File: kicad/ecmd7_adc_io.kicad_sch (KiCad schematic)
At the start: 84 parts, among them U10 FIN1002M5X, U11 FIN1002M5X, U12 FIN1002M5X, U13 ADM3490ExR, U15 74LVC1G139, U16 MB85RS1MT, U17 TMP122AIDBVR, U2 MCP33151-05T-E/MN, U4 MCP33151-05T-E/MN, U5 MCP33151-05T-E/MN, U7 MCP33151-05T-E/MN

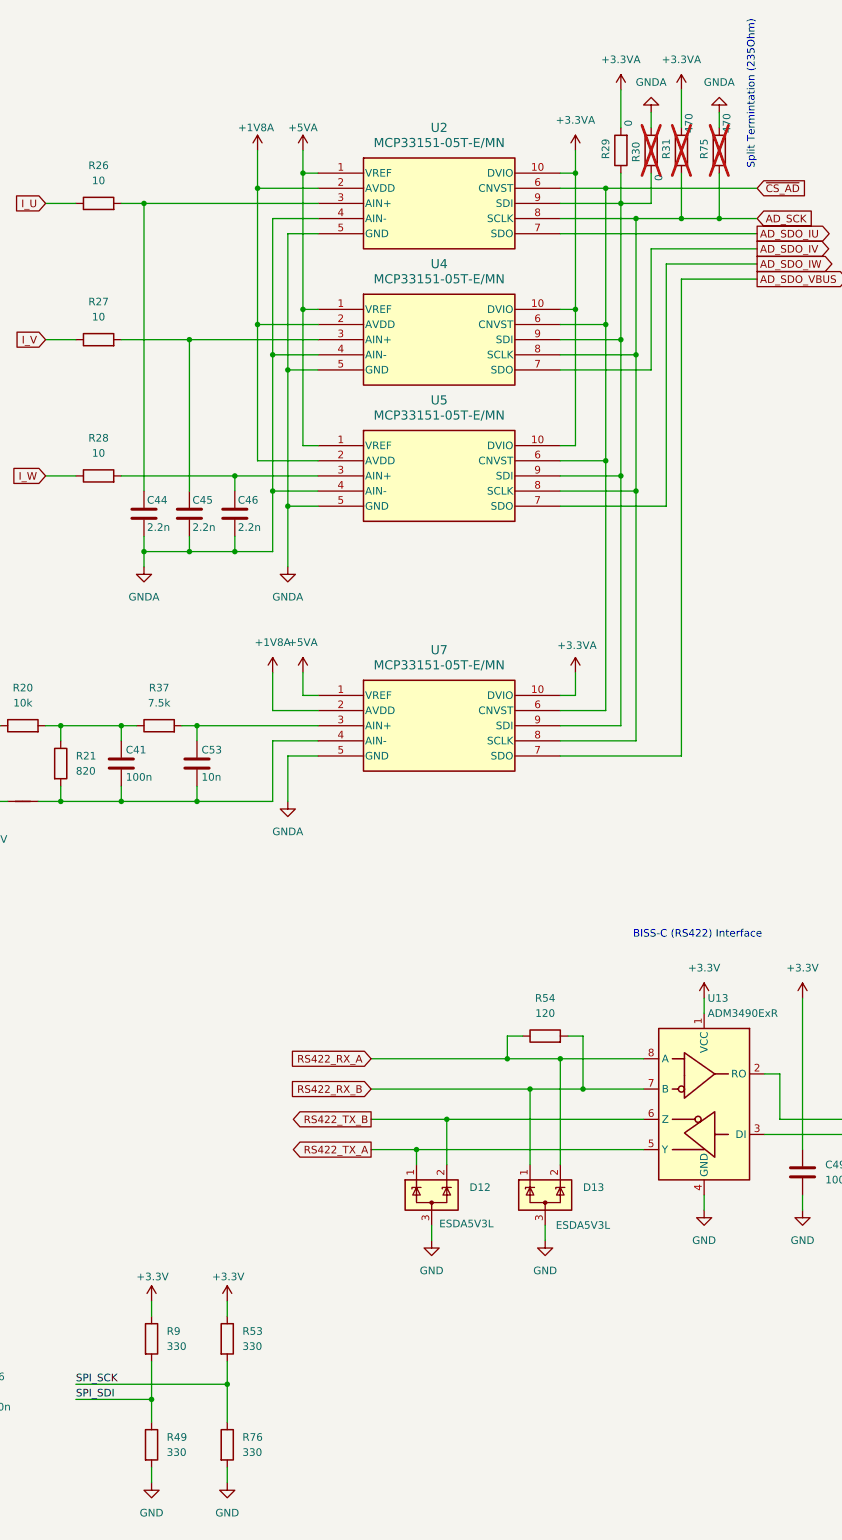
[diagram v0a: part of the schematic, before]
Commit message: Update project structure for enhancment with firmware and software
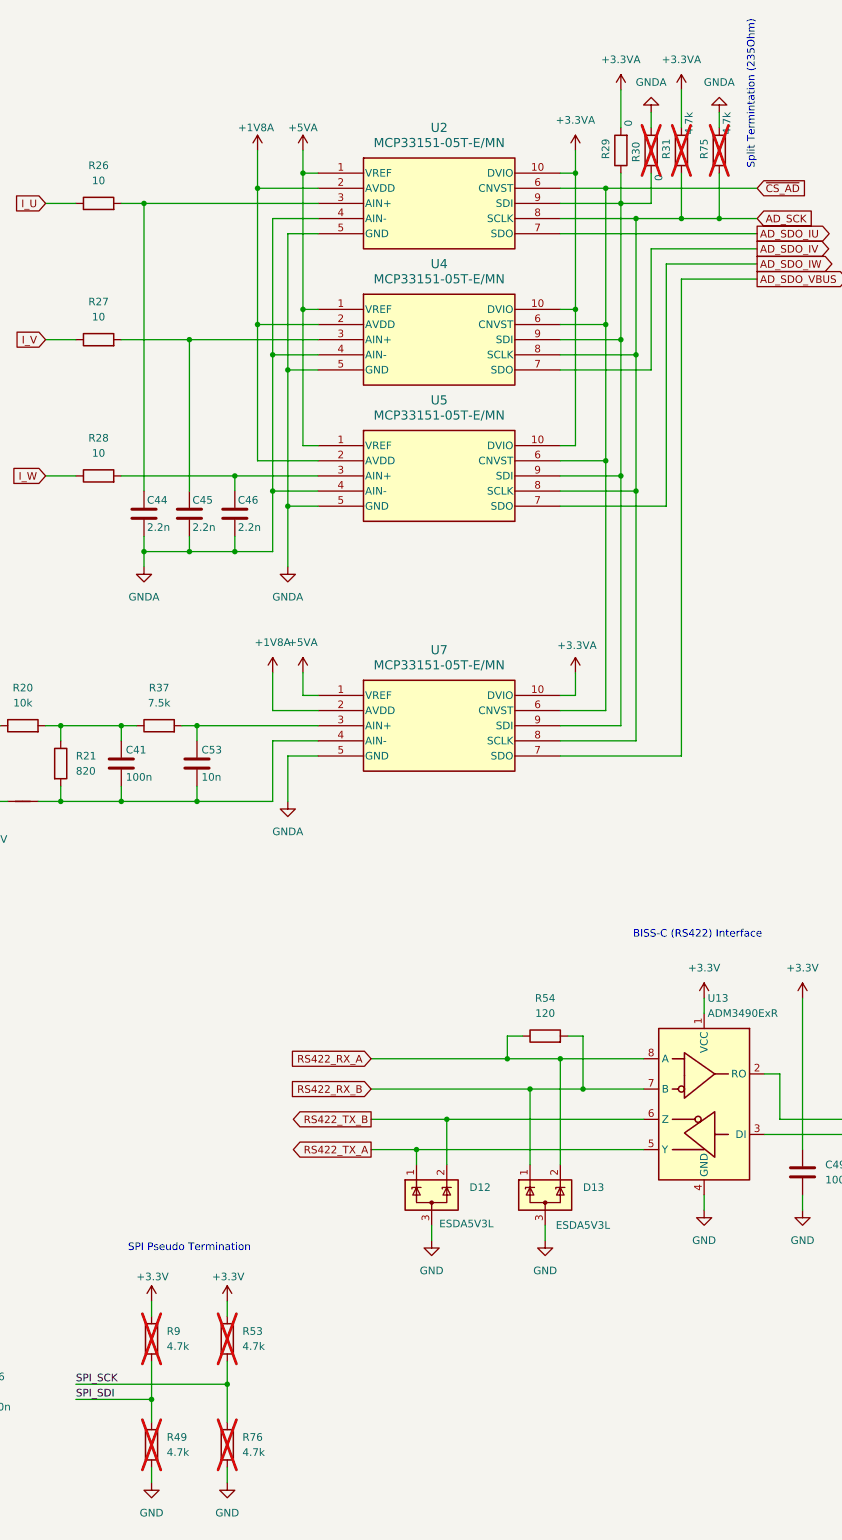
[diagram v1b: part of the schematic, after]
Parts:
- D10, D11, D12, D13, D9: Mouser Part Number (none) -> 511-ESDA5V3L
- R31, R75: value 470 -> 4.7k
- R49, R53, R76, R9: value 330 -> 4.7k; now not fitted
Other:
- note added: "SPI Pseudo Termination"
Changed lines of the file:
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@@
 		(rev "0,0")
 	)
+	(text "SPI Pseudo Termination"
+		(exclude_from_sim no)
+		(at 247.65 222.25 0)
+		(effects
+			(font
+				(size 1.27 1.27)
+			)
+		)
+	)
 	(text "BISS-C (RS422) Interface"
 		(exclude_from_sim no)
@@
 		(in_bom yes)
 		(on_board yes)
-		(dnp no)
+		(dnp yes)
 		(fields_autoplaced yes)
 		(property "Reference" "R53"
@@
 			)
 		)
-		(property "Value" "330"
+		(property "Value" "4.7k"
 			(at 256.54 238.7599 0)
 			(effects
@@
 			)
 		)
+		(property "Mouser Part Number" "511-ESDA5V3L"
+			(at 63.5 181.61 0)
+			(effects
+				(font
+					(size 1.27 1.27)
+				)
+				(hide yes)
+			)
+		)
 		(pin "3"
 		)
@@
 			)
 		)
-		(property "Value" "470"
+		(property "Value" "4.7k"
 			(at 331.47 33.528 90)
 			(effects
@@
 		(in_bom yes)
 		(on_board yes)
-		(dnp no)
+		(dnp yes)
 		(fields_autoplaced yes)
 		(property "Reference" "R9"
@@
 			)
 		)
-		(property "Value" "330"
+		(property "Value" "4.7k"
 			(at 243.84 238.7599 0)
 			(effects
@@
 			)
 		)
+		(property "Mouser Part Number" "511-ESDA5V3L"
+			(at 307.34 213.36 0)
+			(effects
+				(font
+					(size 1.27 1.27)
+				)
+				(hide yes)
+			)
+		)
 		(pin "3"
 		)
@@
 			)
 		)
-		(property "Value" "470"
+		(property "Value" "4.7k"
 			(at 337.82 33.528 90)
 			(effects
@@
 		(in_bom yes)
 		(on_board yes)
-		(dnp no)
+		(dnp yes)
 		(fields_autoplaced yes)
 		(property "Reference" "R76"
@@
 			)
 		)
-		(property "Value" "330"
+		(property "Value" "4.7k"
 			(at 256.54 256.5399 0)
 			(effects
@@
 			)
 		)
+		(property "Mouser Part Number" "511-ESDA5V3L"
+			(at 63.5 68.58 0)
+			(effects
+				(font
+					(size 1.27 1.27)
+				)
+				(hide yes)
+			)
+		)
 		(pin "3"
 		)
@@
 			)
 		)
+		(property "Mouser Part Number" "511-ESDA5V3L"
+			(at 63.5 125.73 0)
+			(effects
+				(font
+					(size 1.27 1.27)
+				)
+				(hide yes)
+			)
+		)
 		(pin "3"
 		)
@@
 			)
 		)
+		(property "Mouser Part Number" "511-ESDA5V3L"
+			(at 288.29 213.36 0)
+			(effects
+				(font
+					(size 1.27 1.27)
+				)
+				(hide yes)
+			)
+		)
 		(pin "3"
 		)
@@
 		(in_bom yes)
 		(on_board yes)
-		(dnp no)
+		(dnp yes)
 		(fields_autoplaced yes)
 		(property "Reference" "R49"
@@
 			)
 		)
-		(property "Value" "330"
+		(property "Value" "4.7k"
 			(at 243.84 256.5399 0)
 			(effects

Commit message: Cleanup schematic
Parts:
- removed C11, C51, C52, C56, C58, C59, C60, C76: 100n, Capacitor_SMD:C_0805_2012Metric, symbol Device:C
- removed C49: 100n, Capacitor_SMD:C_0603_1608Metric, symbol Device:C
- removed D10, D11, D12, D13, D9: ESDA5V3L, Package_TO_SOT_SMD:SOT-23-3, symbol Power_Protection:ESDA5V3L
- removed JP10: ~{WP}=1, Jumper:SolderJumper-2_P1.3mm_Bridged_RoundedPad1.0x1.5mm, symbol Jumper:SolderJumper_2_Bridged
- removed JP12: ~{WP}=0, Jumper:SolderJumper-2_P1.3mm_Open_RoundedPad1.0x1.5mm, symbol Jumper:SolderJumper_2_Open
- removed R22, R23, R24, R25, R39, R40: 3.9k, Resistor_SMD:R_0805_2012Metric, symbol Device:R
- removed R32, R38, R43, R55, R58, R60: 820, Resistor_SMD:R_0805_2012Metric, symbol Device:R
- removed R33, R36, R42: 330, Resistor_SMD:R_0805_2012Metric, symbol Device:R
- removed R34, R35, R41, R56, R57, R59: 1.8k, Resistor_SMD:R_0805_2012Metric, symbol Device:R
- removed R49, R53, R76, R9: 4.7k, Resistor_SMD:R_0805_2012Metric, symbol Device:R
- removed R54: 120, Resistor_SMD:R_0805_2012Metric, symbol Device:R
- removed R61, R62, R63: 100k, Resistor_SMD:R_0805_2012Metric, symbol Device:R
- removed U10, U11, U12: FIN1002M5X, Package_TO_SOT_SMD:SOT-23-5, symbol SSTA:FIN1002M5X
- removed U13: ADM3490ExR, Package_SO:SOIC-8_3.9x4.9mm_P1.27mm, symbol Interface_UART:ADM3490ExR
- removed U15: 74LVC1G139, Package_SO:SSOP-8_2.95x2.8mm_P0.65mm, symbol 74xGxx:74LVC1G139
- removed U16: MB85RS1MT, Package_SO:SOP-8_3.76x4.96mm_P1.27mm, symbol Memory_NVRAM:MB85RS1MT
- removed U17: TMP122AIDBVR, SSTA:DBV6, symbol SSTA:TMP122AIDBVR
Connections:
- no-connect marks 2 -> 0
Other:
- note removed: "BISS-C (RS422) Interface"
- note removed: "Inputs can be configured for differential quadrature encoder signals or hall switches. Default configuration is for differential 5V TTL quadrature encoder inputs"
- note removed: "SPI Pseudo Termination"
- moved on the sheet: C1, C10, C2, C3, C4, C41, C44, C45, C46, C47, C5, C50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

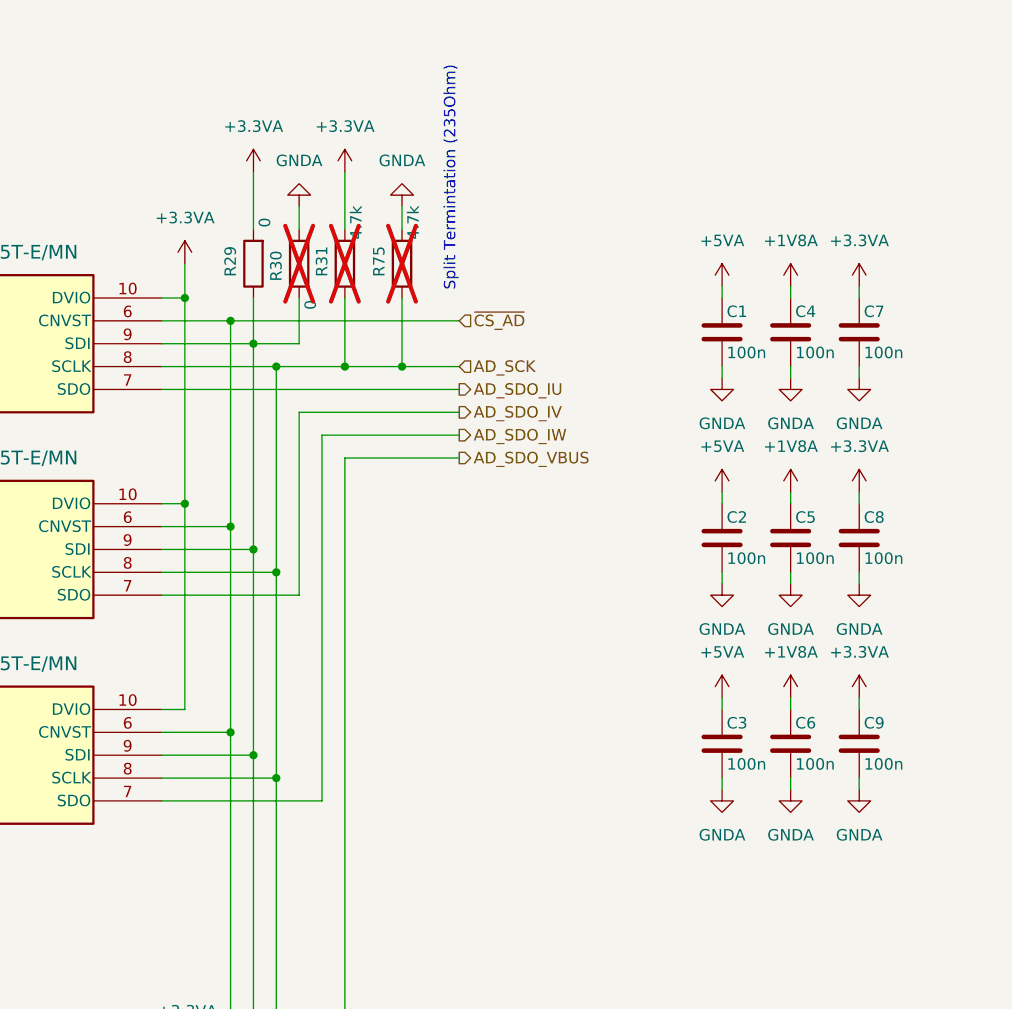
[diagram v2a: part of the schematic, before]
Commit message: Cleanup schematic, add busses
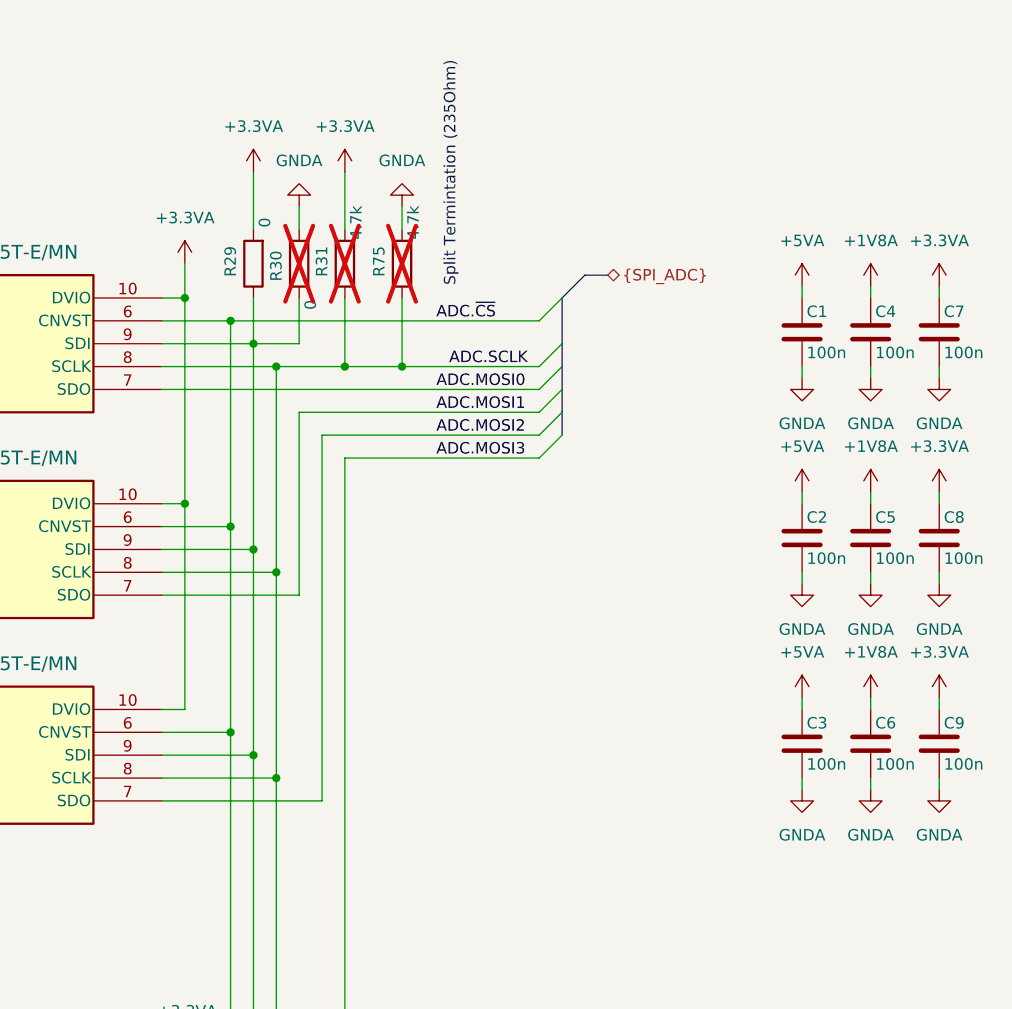
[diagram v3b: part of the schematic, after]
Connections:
- net AD_SCK renamed ADC.SCLK
- net AD_SDO_IU renamed ADC.MOSI0
- net AD_SDO_IV renamed ADC.MOSI1
- net AD_SDO_IW renamed ADC.MOSI2
- net AD_SDO_VBUS renamed ADC.MOSI3
- net ~{CS_AD} renamed ADC.~{CS}
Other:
- title: ECMD7 Feedback -> ECMD7 Current + Voltage Feedback ADC
- moved on the sheet: C1, C2, C3, C4, C5, C6, C7, C8, C9

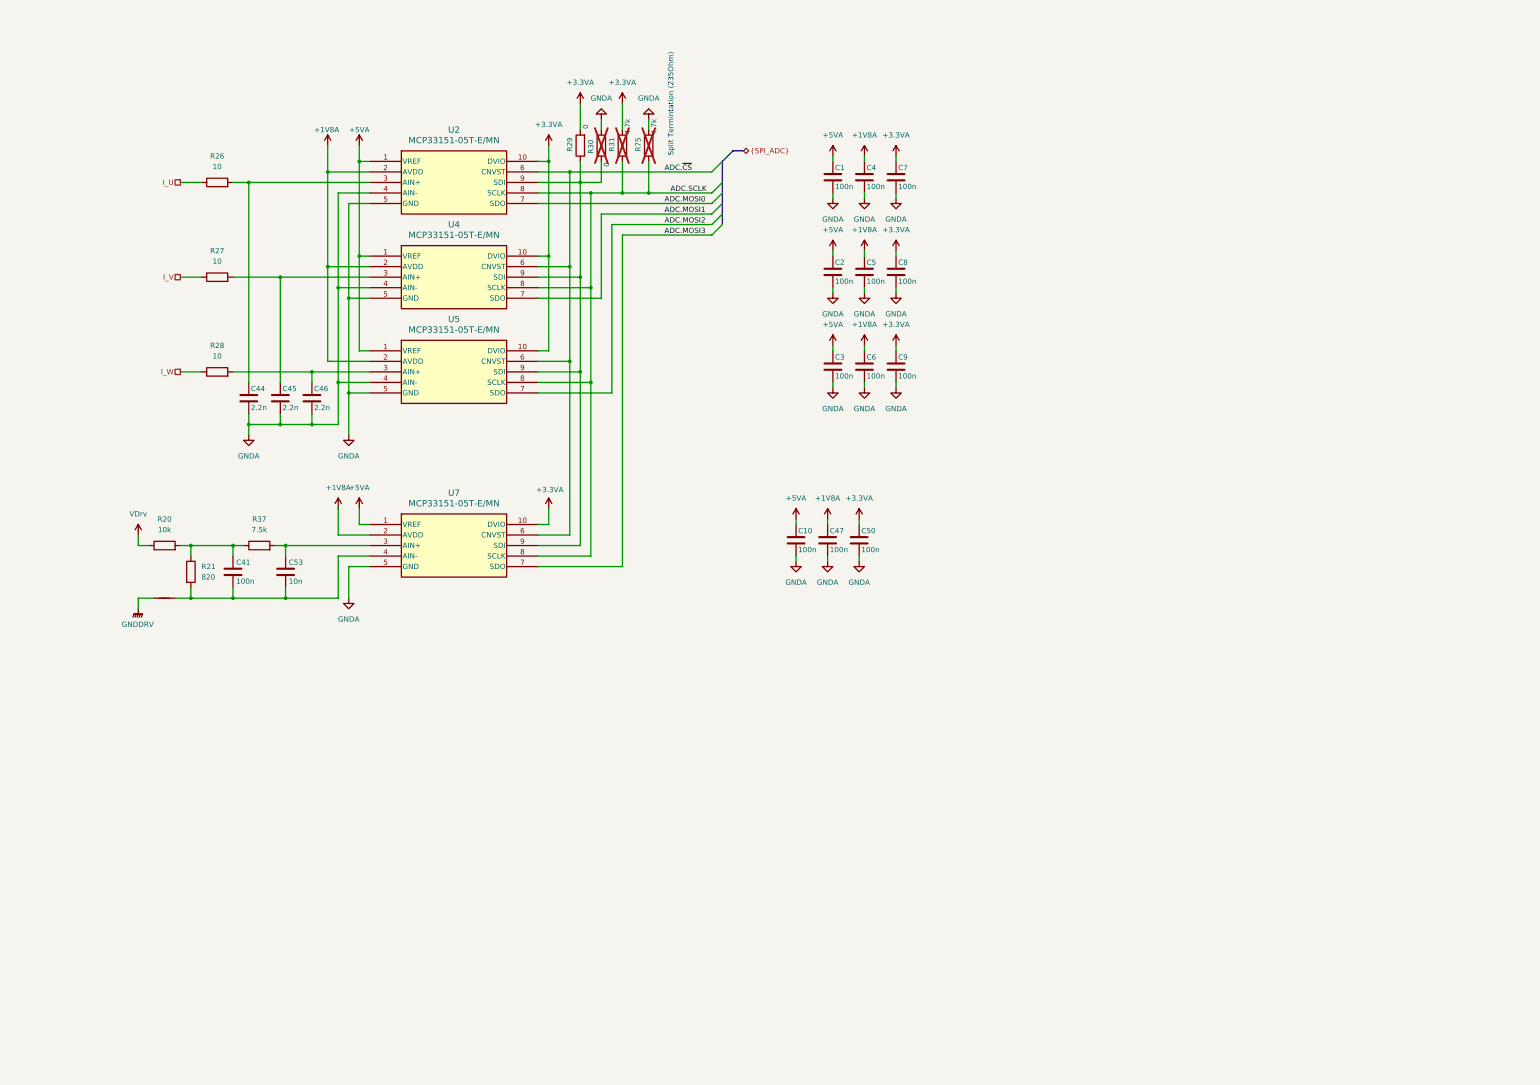
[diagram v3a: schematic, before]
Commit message: General schematic cleanup
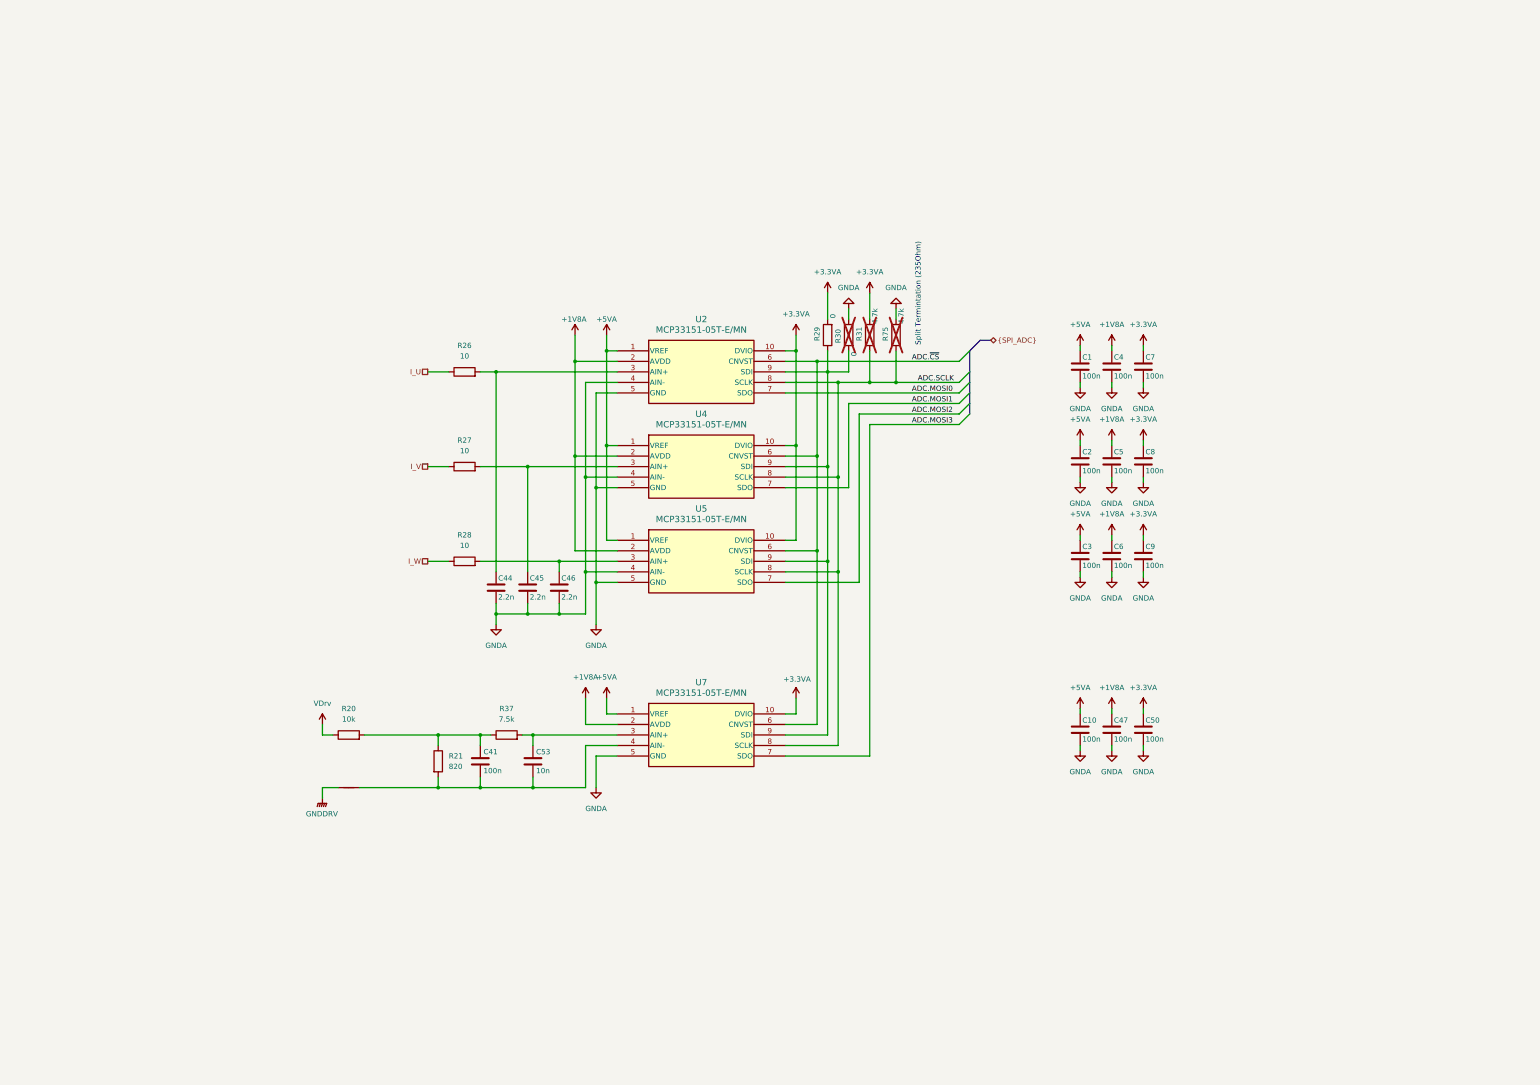
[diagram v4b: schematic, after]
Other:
- moved on the sheet: C1, C10, C2, C3, C4, C41, C44, C45, C46, C47, C5, C50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
